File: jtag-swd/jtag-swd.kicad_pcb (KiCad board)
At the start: 2 copper layers, 16.5 x 12.7 mm, 3 parts, among them J1 Conn_ARM_JTAG_SWD_10, J2 Conn_01x04_Male, J3 Conn_01x02_Male

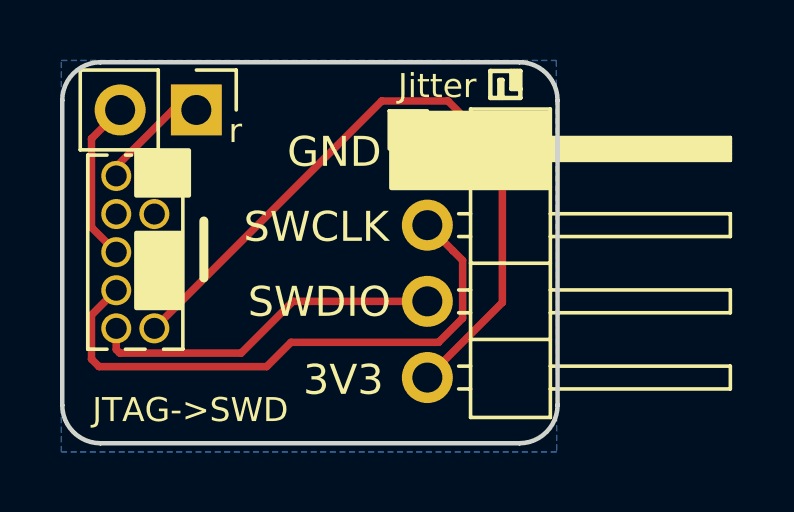
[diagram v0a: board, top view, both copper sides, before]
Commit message: Modernize the adapter boards
This repo contains adapter boards for the Jitter 6-pins REDFit debug
interface to multiple standard programming/debug tools.
Each now renamed to make this clearer (BMP/HSProbe/JLink) and save those
projects as modern Kicad10 designs
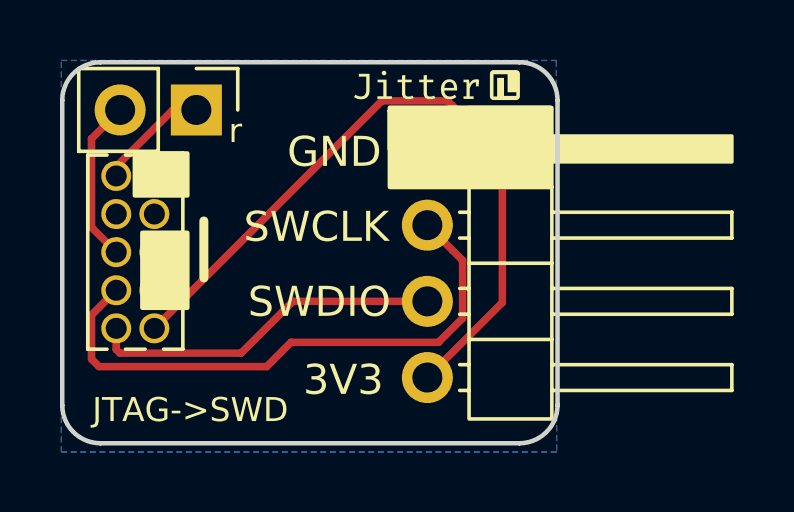
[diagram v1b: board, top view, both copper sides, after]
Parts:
- added LOGO1: LOGO, Jitter_Logos:Jitter-micro, F.Cu at (85.5, 42.6)
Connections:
- J1 pad 7: (no net) -> unconnected-(J1-KEY-Pad7)
- J1 pad 8: (no net) -> unconnected-(J1-NC/TDI-Pad8)
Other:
- net class Default removed
- rule pad_to_mask_clearance: 0.051 -> 0
- rule solder_mask_min_width: 0.25 -> 0.2
- board text removed: "Jitter"
